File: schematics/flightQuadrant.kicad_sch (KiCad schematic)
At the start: 13 parts, among them J1 Jack-DC, M1 M_ENG1, M2 M_ENG2, M3 M_BRK, M4 M_FLP, U1 L293D, U2 L293D

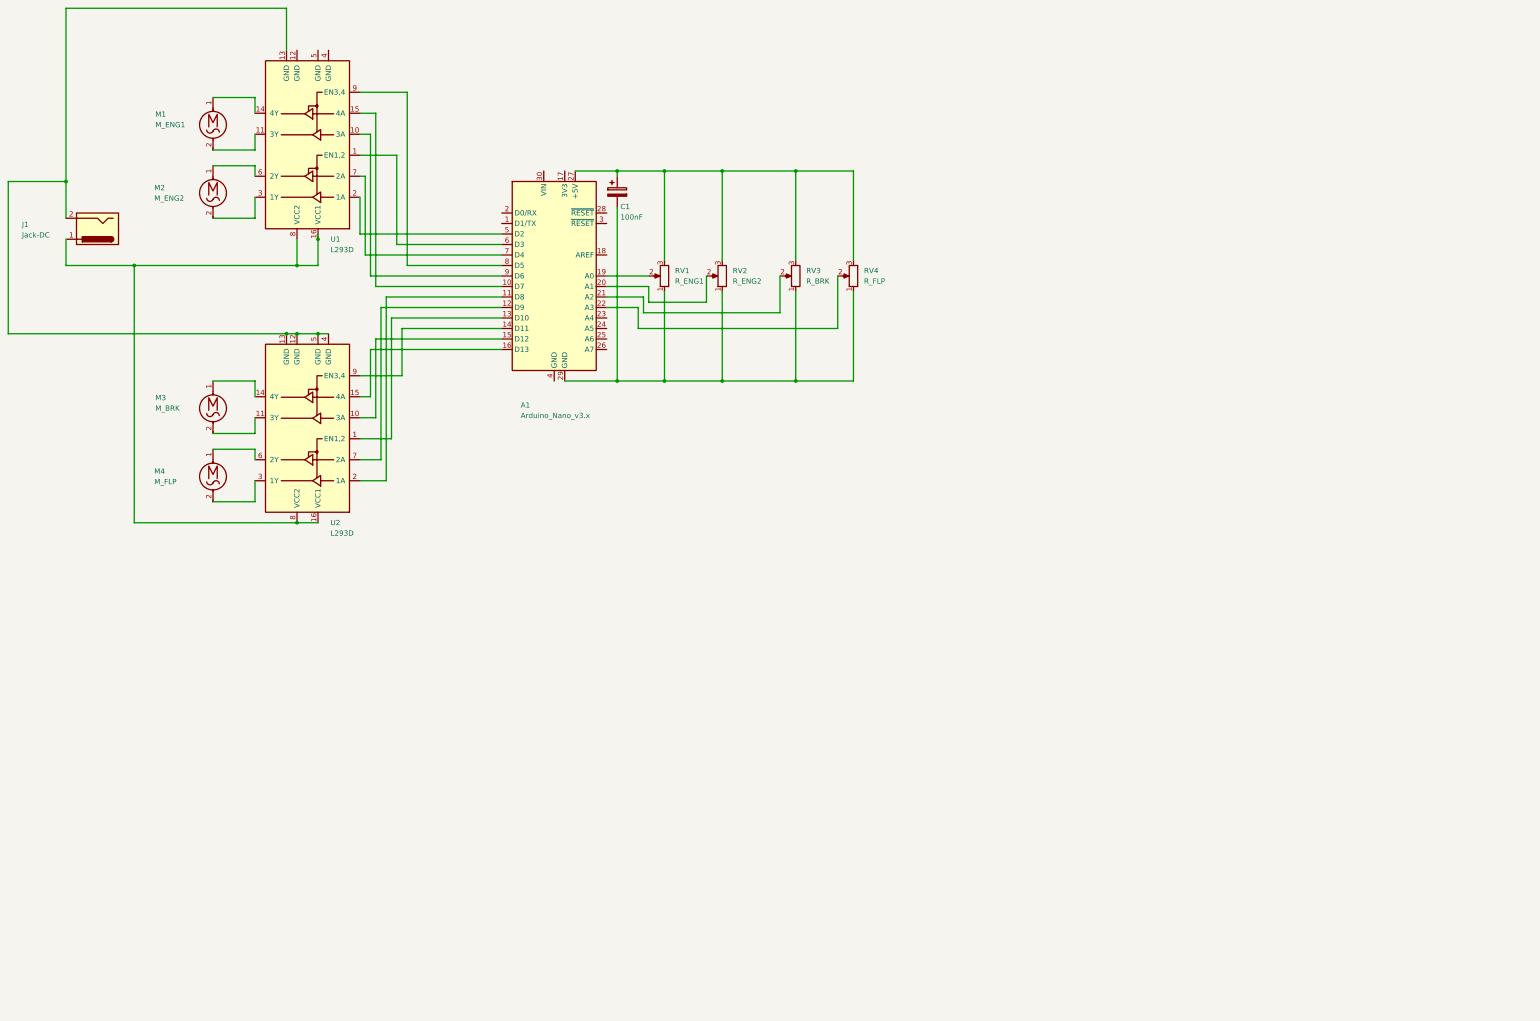
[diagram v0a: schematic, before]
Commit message: Migrate to teeensyyyy 3.2
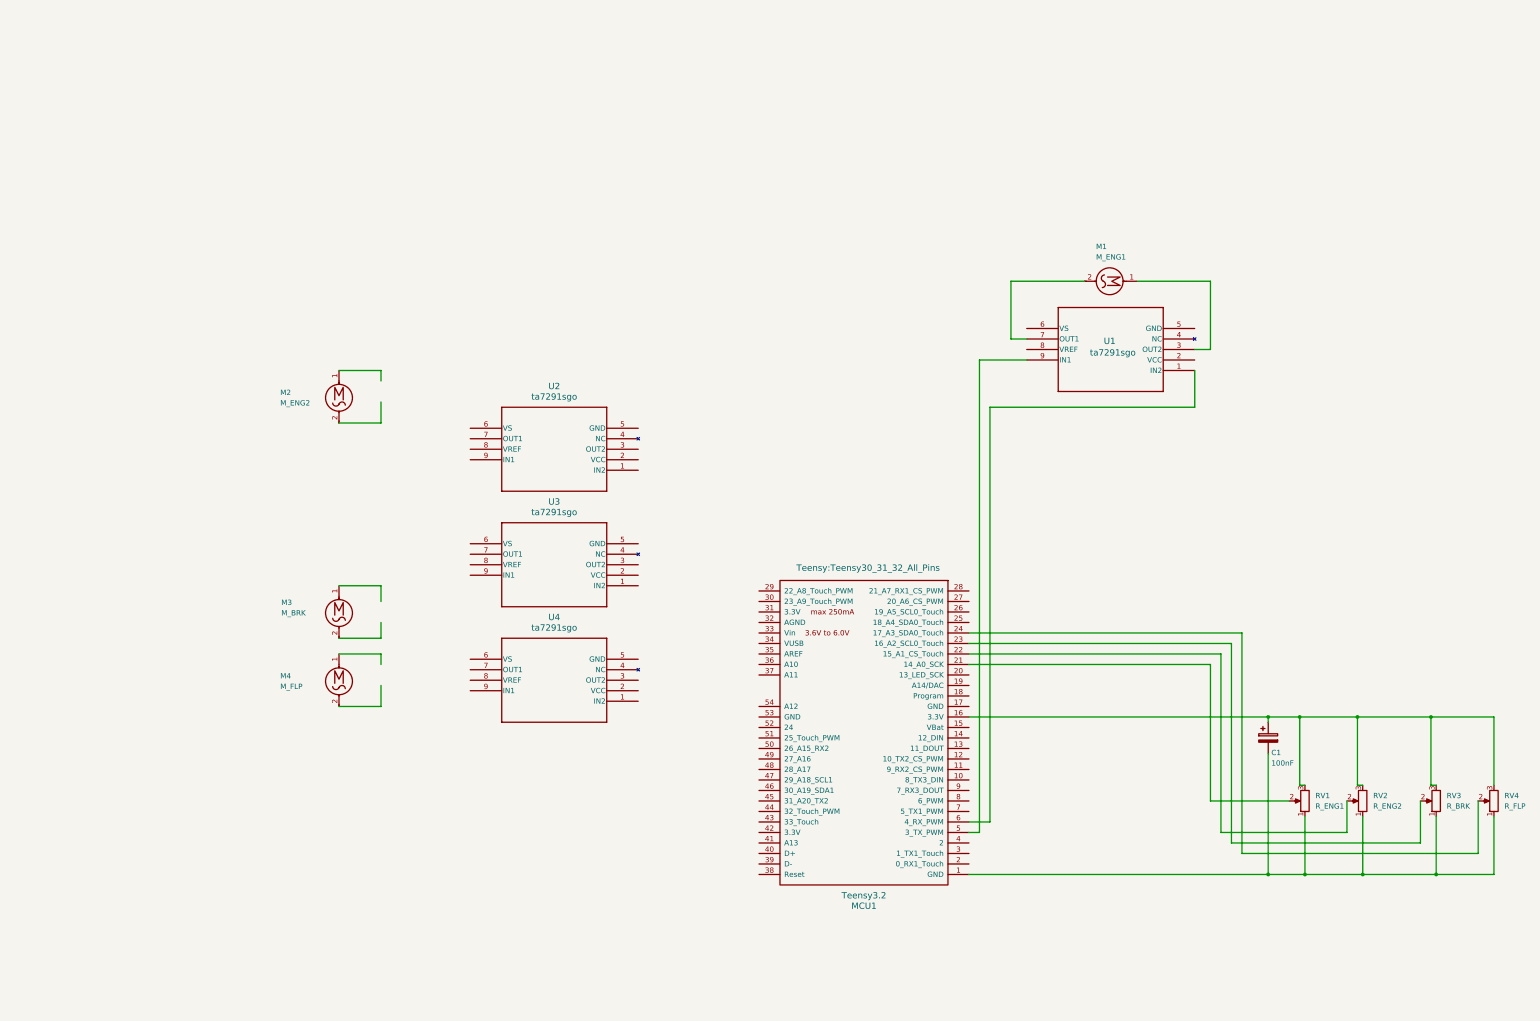
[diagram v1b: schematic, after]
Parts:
- removed A1: Arduino_Nano_v3.x, Module:Arduino_Nano, symbol MCU_Module:Arduino_Nano_v3.x
- removed J1: Jack-DC, Connector_BarrelJack:BarrelJack_GCT_DCJ200-10-A_Horizontal, symbol Connector:Jack-DC
- removed U1, U2: L293D, Package_DIP:DIP-16_W7.62mm, symbol Driver_Motor:L293D
- added MCU1: Teensy3.2, Teensy:Teensy30_31_32_All_Pins, symbol Teensy:Teensy3.2
- added U1, U2, U3, U4: ta7291sgo, SIP9_TOS, symbol Driver Pot:ta7291sgo
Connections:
- net at C1.1, RV1.3, RV2.3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: now also MCU1.16 (3.3V)
- net at C1.2, RV1.1, RV2.1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: now also MCU1.1 (GND)
- net at M1.2: now also U1.7 (OUT1)
- net at M1.1: now also U1.3 (OUT2)
- net at RV1.2: now also MCU1.21 (14_A0_SCK)
- net at RV2.2: now also MCU1.22 (15_A1_CS_Touch)
- net at RV3.2: now also MCU1.23 (16_A2_SCL0_Touch)
- net at RV4.2: now also MCU1.24 (17_A3_SDA0_Touch)
- new net: MCU1.6 (4_RX_PWM), U1.1 (IN2)
- new net: MCU1.5 (3_TX_PWM), U1.9 (IN1)
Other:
- moved on the sheet: C1, M1, M2, M3, M4, RV1, RV2, RV3, RV4

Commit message: Update arduino code firmware!
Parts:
- added C2: C, symbol Device:C
- added C3: C_Polarized, symbol Device:C_Polarized
- added J1: Barrel_Jack, symbol Connector:Barrel_Jack
- C1: value 100nF -> C_Polarized; footprint Capacitor_THT:CP_Radial_D5.0mm_P2.00mm -> (none)
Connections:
- net at U1.2 (VCC): now also U1.6 (VS), C3.2, J1.1
- net at M1.1, U1.3 (OUT2): now also C2.2
- net at U1.5 (GND): now also C1.2, MCU1.1 (GND), RV1.1, RV2.1, RV3.1, RV4.1, C3.1, J1.2
- net at M1.2, U1.7 (OUT1): now also C2.1
- net at U1.8 (VREF): now also MCU1.31 (3.3V)
- net at U2.3 (OUT2): now also M2.1
- net at U2.7 (OUT1): now also M2.2
- no-connect marks 0 -> 1
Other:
- moved on the sheet: M1, M2, M3, M4, MCU1, RV1, RV2, RV3, RV4, U1, U2, U3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
